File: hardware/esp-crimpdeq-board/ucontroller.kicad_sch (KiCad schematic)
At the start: 11 parts, among them U8 ESP32-C6-MINI-1/U, Y1 32.768Hz

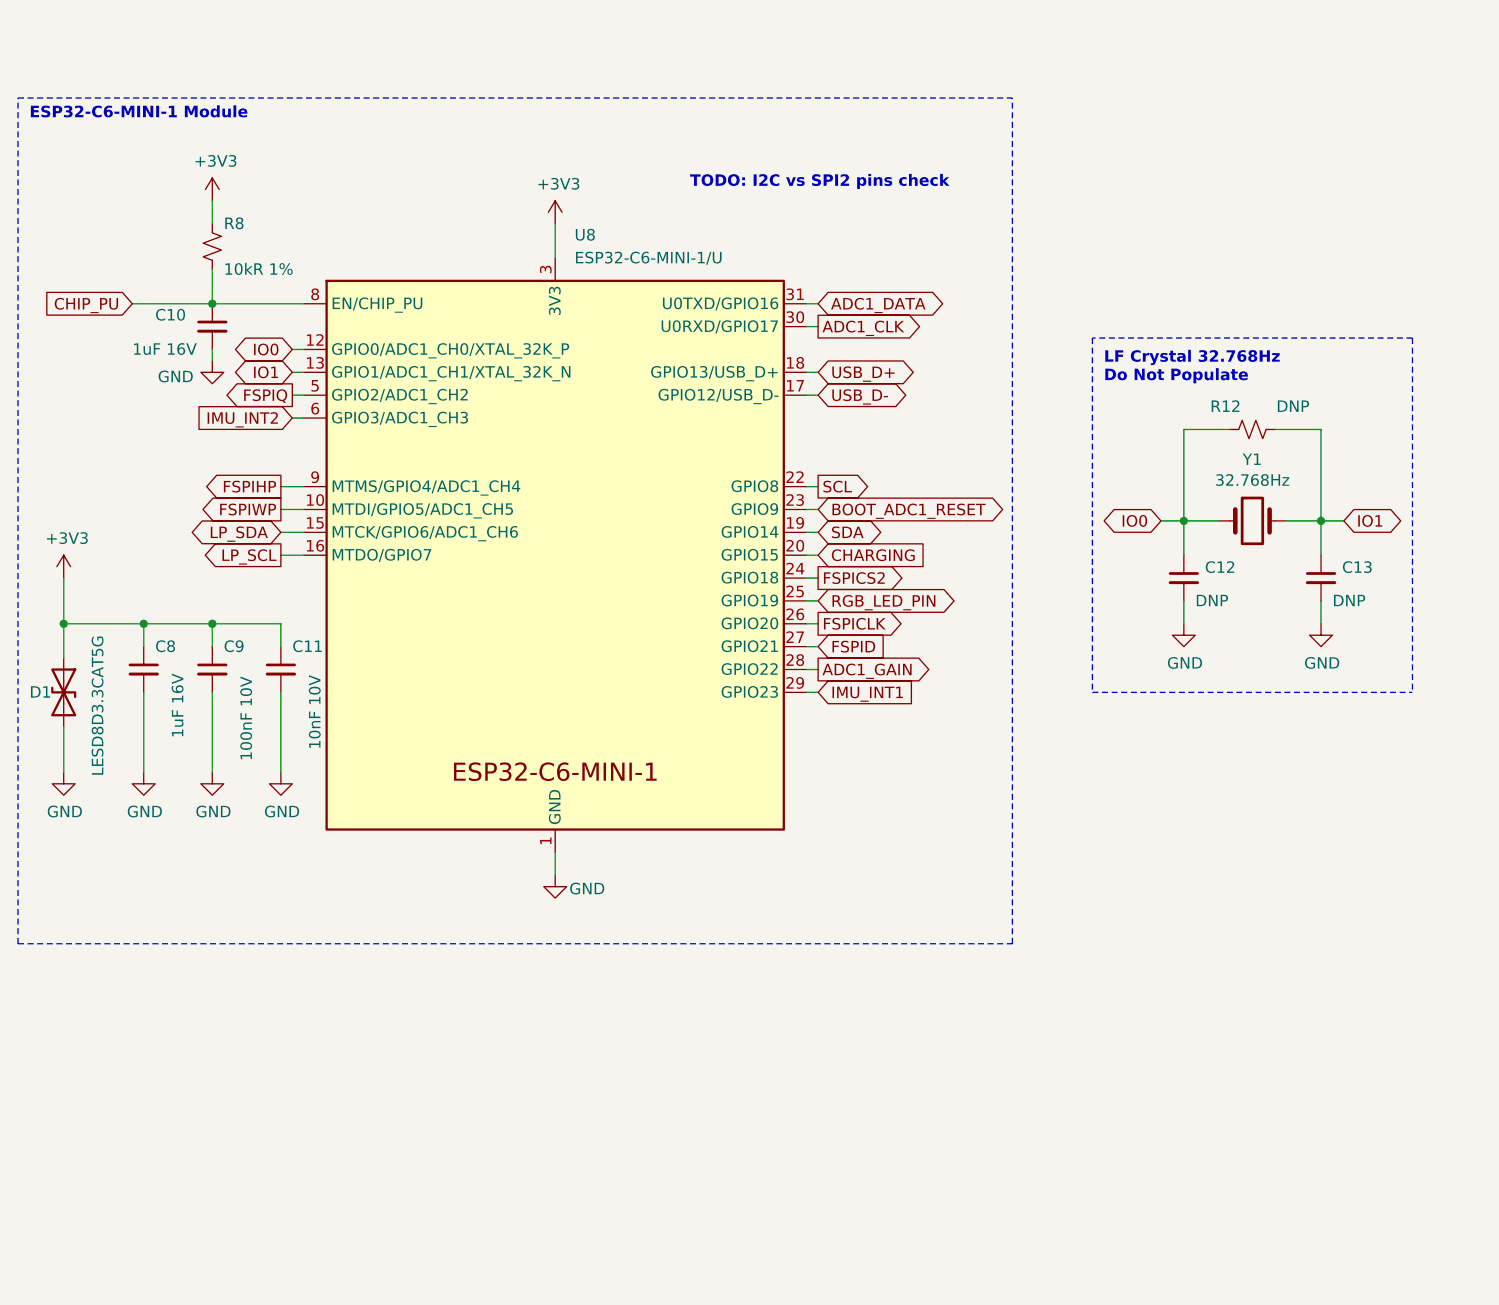
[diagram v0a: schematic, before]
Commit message: Ordering sdchematic in different sheets
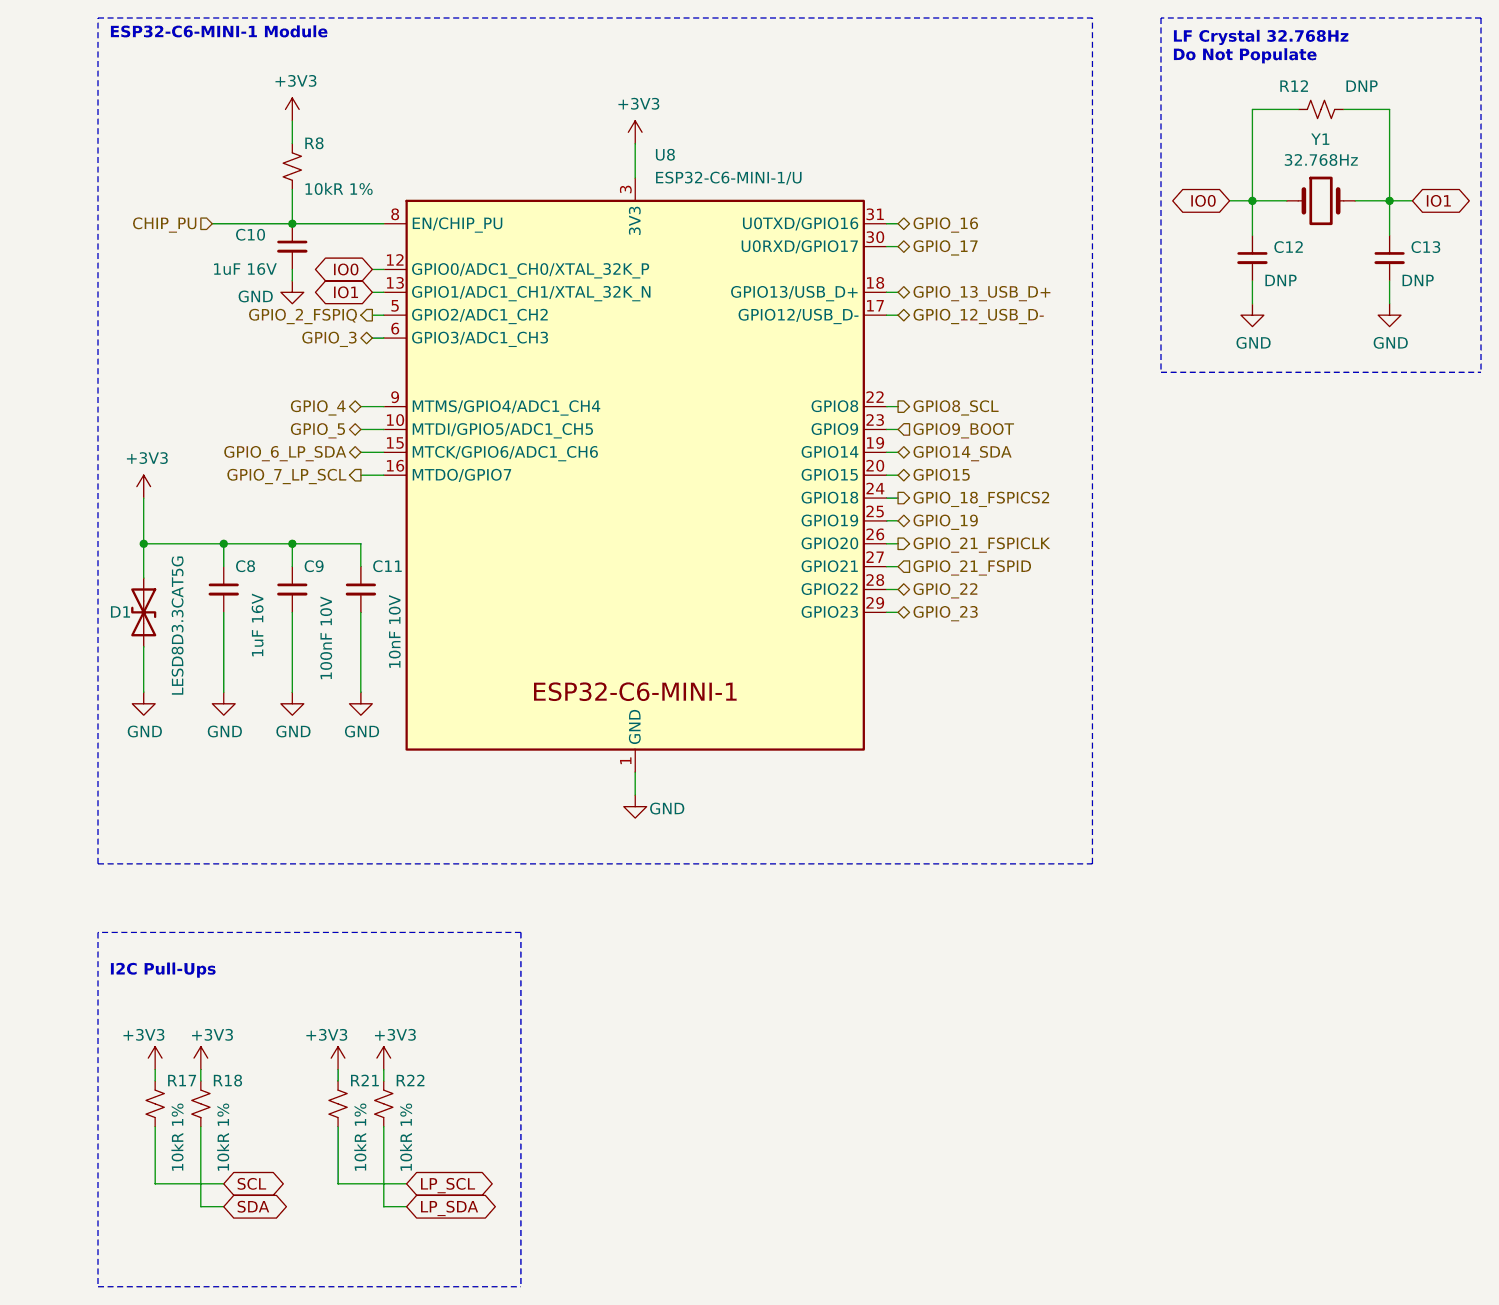
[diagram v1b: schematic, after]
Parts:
- added R17, R18, R21, R22: 10kR 1%, Resistor_SMD:R_0402_1005Metric, symbol Device:R_Small_US
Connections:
- net +3V3: now also R17.1, R18.1, R21.1, R22.1
- net LP_SCL: now also R21.2; no longer U8.16 (MTDO/GPIO7)
- net LP_SDA: now also R22.2; no longer U8.15 (MTCK/GPIO6/ADC1_CH6)
- net SCL: now also R17.2; no longer U8.22 (GPIO8)
- net SDA: now also R18.2; no longer U8.19 (GPIO14)
- net ADC1_CLK renamed GPIO_17
- net ADC1_DATA renamed GPIO_16
- net ADC1_GAIN renamed GPIO_22
- net BOOT_ADC1_RESET renamed GPIO9_BOOT
- net CHARGING renamed GPIO15
- net FSPICLK renamed GPIO_21_FSPICLK
- net FSPICS2 renamed GPIO_18_FSPICS2
- net FSPID renamed GPIO_21_FSPID
- net FSPIHP renamed GPIO_4
- net FSPIQ renamed GPIO_2_FSPIQ
- net FSPIWP renamed GPIO_5
- net IMU_INT1 renamed GPIO_23
- net IMU_INT2 renamed GPIO_3
- net RGB_LED_PIN renamed GPIO_19
- net USB_D+ renamed GPIO_13_USB_D+
- net USB_D- renamed GPIO_12_USB_D-
- new net GPIO14_SDA: U8.19 (GPIO14)
- new net GPIO8_SCL: U8.22 (GPIO8)
- new net GPIO_6_LP_SDA: U8.15 (MTCK/GPIO6/ADC1_CH6)
- new net GPIO_7_LP_SCL: U8.16 (MTDO/GPIO7)
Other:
- note added: "I2C Pull-Ups"
- note removed: "TODO: I2C vs SPI2 pins check"
- moved on the sheet: C10, C11, C12, C13, C8, C9, D1, R12, R8, U8, Y1
